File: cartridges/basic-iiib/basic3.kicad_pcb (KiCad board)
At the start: 2 copper layers, 72 x 37.3 mm, 10 parts, among them SW1 SW_SPDT, U1 27C512, U2 SG-1000-Cart, U3 UM61512

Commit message: Plotted - v0.1 released
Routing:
- net /GND: track 37.2 -> 62.5 mm, vias 6 -> 7
- net /D6: track 104.7 -> 105.8 mm
- removed copper zone on F.Cu, net /GND
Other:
- board size 72 x 37.3 mm -> 72 x 39.8 mm
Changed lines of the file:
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@@
   (gr_rect (start 189.484 135.89) (end 116.713 122.809) (layer "B.Mask") (width 0.15) (fill solid))
   (gr_rect (start 189.484 122.809) (end 116.713 136.398) (layer "F.Mask") (width 0.15) (fill solid))
-  (gr_line (start 189.238 122.686) (end 189.23 86.995) (layer "Edge.Cuts") (width 0.1))
-  (gr_line (start 117.238 124.286) (end 117.2464 86.995) (layer "Edge.Cuts") (width 0.1))
-  (gr_line (start 117.2464 86.995) (end 189.23 86.995) (layer "Edge.Cuts") (width 0.1))
+  (gr_line (start 189.238 122.686) (end 189.23 84.455) (layer "Edge.Cuts") (width 0.1))
+  (gr_line (start 117.238 124.286) (end 117.2464 84.455) (layer "Edge.Cuts") (width 0.1))
+  (gr_line (start 117.2464 84.455) (end 189.23 84.455) (layer "Edge.Cuts") (width 0.1))
   (gr_line (start 189.238 122.686) (end 189.238 124.286) (layer "Edge.Cuts") (width 0.1))
   (gr_text "A22" (at 186.436 120.904) (layer "B.SilkS")
@@
   (segment (start 172.72 113.665) (end 173.355 113.03) (width 0.75) (layer "B.Cu") (net 1))
   (segment (start 168.91 104.79) (end 172.07 104.79) (width 0.75) (layer "F.Cu") (net 2))
+  (segment (start 184.785 116.84) (end 183.515 116.84) (width 0.75) (layer "F.Cu") (net 2))
+  (segment (start 183.515 127.909) (end 183.338 128.086) (width 0.75) (layer "F.Cu") (net 2))
   (segment (start 172.07 104.79) (end 172.085 104.775) (width 0.75) (layer "F.Cu") (net 2))
+  (segment (start 186.518 128.086) (end 186.518 117.303) (width 0.75) (layer "F.Cu") (net 2))
   (segment (start 172.085 104.775) (end 177.8 104.775) (width 0.75) (layer "F.Cu") (net 2))
-  (via (at 183.515 116.84) (size 0.8) (drill 0.4) (layers "F.Cu" "B.Cu") (free) (net 2))
-  (via (at 183.515 118.11) (size 0.8) (drill 0.4) (layers "F.Cu" "B.Cu") (free) (net 2))
-  (via (at 186.055 118.11) (size 0.8) (drill 0.4) (layers "F.Cu" "B.Cu") (free) (net 2))
-  (via (at 186.055 116.84) (size 0.8) (drill 0.4) (layers "F.Cu" "B.Cu") (free) (net 2))
+  (segment (start 186.055 116.84) (end 184.785 116.84) (width 0.75) (layer "F.Cu") (net 2))
+  (segment (start 183.515 116.84) (end 183.515 118.11) (width 0.75) (layer "F.Cu") (net 2))
+  (segment (start 183.515 119.38) (end 183.515 127.909) (width 0.75) (layer "F.Cu") (net 2))
+  (segment (start 183.515 118.11) (end 183.515 119.38) (width 0.75) (layer "F.Cu") (net 2))
+  (segment (start 186.518 117.303) (end 186.055 116.84) (width 0.75) (layer "F.Cu") (net 2))
+  (via (at 183.515 119.38) (size 0.8) (drill 0.4) (layers "F.Cu" "B.Cu") (net 2))
+  (via (at 183.515 118.11) (size 0.8) (drill 0.4) (layers "F.Cu" "B.Cu") (net 2))
+  (via (at 186.055 116.84) (size 0.8) (drill 0.4) (layers "F.Cu" "B.Cu") (net 2))
+  (via (at 183.515 116.84) (size 0.8) (drill 0.4) (layers "F.Cu" "B.Cu") (net 2))
   (via (at 177.8 104.775) (size 0.8) (drill 0.4) (layers "F.Cu" "B.Cu") (net 2))
+  (via (at 184.785 116.84) (size 0.8) (drill 0.4) (layers "F.Cu" "B.Cu") (net 2))
   (via (at 172.085 104.775) (size 0.8) (drill 0.4) (layers "F.Cu" "B.Cu") (net 2))
   (segment (start 124.990489 94.739511) (end 126.365 93.365) (width 0.75) (layer "B.Cu") (net 2))
@@
   (via (at 186.69 97.79) (size 0.8) (drill 0.4) (layers "F.Cu" "B.Cu") (net 10))
   (via (at 136.525 97.79) (size 0.8) (drill 0.4) (layers "F.Cu" "B.Cu") (net 10))
+  (segment (start 183.96451 120.83549) (end 184.785 120.015) (width 0.25) (layer "B.Cu") (net 10))
   (segment (start 136.515 105.42) (end 136.515 118.74) (width 0.25) (layer "B.Cu") (net 10))
-  (segment (start 182.88 121.92) (end 184.785 120.015) (width 0.25) (layer "B.Cu") (net 10))
   (segment (start 136.525 99.695) (end 136.525 101.9197) (width 0.25) (layer "B.Cu") (net 10))
-  (segment (start 181.61 121.92) (end 182.88 121.92) (width 0.25) (layer "B.Cu") (net 10))
-  (segment (start 184.785 120.015) (end 186.055 120.015) (width 0.25) (layer "B.Cu") (net 10))
+  (segment (start 180.158 128.086) (end 180.158 123.372) (width 0.25) (layer "B.Cu") (net 10))
   (segment (start 136.525 97.79) (end 136.525 99.695) (width 0.25) (layer "B.Cu") (net 10))
-  (segment (start 180.158 123.372) (end 181.61 121.92) (width 0.25) (layer "B.Cu") (net 10))
+  (segment (start 180.158 123.372) (end 182.69451 120.83549) (width 0.25) (layer "B.Cu") (net 10))
   (segment (start 137.639511 103.034211) (end 137.639511 104.295489) (width 0.25) (layer "B.Cu") (net 10))
   (segment (start 136.525 101.9197) (end 137.639511 103.034211) (width 0.25) (layer "B.Cu") (net 10))
-  (segment (start 187.325 118.745) (end 187.325 98.425) (width 0.25) (layer "B.Cu") (net 10))
+  (segment (start 182.69451 120.83549) (end 183.96451 120.83549) (width 0.25) (layer "B.Cu") (net 10))
   (segment (start 187.325 98.425) (end 186.69 97.79) (width 0.25) (layer "B.Cu") (net 10))
-  (segment (start 180.158 128.086) (end 180.158 123.372) (width 0.25) (layer "B.Cu") (net 10))
   (segment (start 186.055 120.015) (end 187.325 118.745) (width 0.25) (layer "B.Cu") (net 10))
   (segment (start 137.639511 104.295489) (end 136.515 105.42) (width 0.25) (layer "B.Cu") (net 10))
+  (segment (start 184.785 120.015) (end 186.055 120.015) (width 0.25) (layer "B.Cu") (net 10))
+  (segment (start 187.325 118.745) (end 187.325 98.425) (width 0.25) (layer "B.Cu") (net 10))
   (segment (start 181.9996 96.52) (end 181.2751 97.2445) (width 0.25) (layer "F.Cu") (net 11))
   (segment (start 187.325 96.52) (end 181.9996 96.52) (width 0.25) (layer "F.Cu") (net 11))
@@
   (segment (start 140.179511 103.034211) (end 140.179511 104.295489) (width 0.25) (layer "B.Cu") (net 11))
   (segment (start 140.179511 104.295489) (end 139.055 105.42) (width 0.25) (layer "B.Cu") (net 11))
-  (segment (start 183.338 124.002704) (end 187.77451 119.566194) (width 0.25) (layer "B.Cu") (net 11))
+  (segment (start 187.77451 119.566194) (end 187.77451 119.56549) (width 0.25) (layer "B.Cu") (net 11))
+  (segment (start 184.15 121.285) (end 186.055704 121.285) (width 0.25) (layer "B.Cu") (net 11))
   (segment (start 187.96 119.38) (end 187.96 97.155) (width 0.25) (layer "B.Cu") (net 11))
   (segment (start 139.065 101.9197) (end 140.179511 103.034211) (width 0.25) (layer "B.Cu") (net 11))
-  (segment (start 187.77451 119.566194) (end 187.77451 119.56549) (width 0.25) (layer "B.Cu") (net 11))
   (segment (start 139.065 99.695) (end 139.065 101.9197) (width 0.25) (layer "B.Cu") (net 11))
-  (segment (start 183.338 128.086) (end 183.338 124.002704) (width 0.25) (layer "B.Cu") (net 11))
+  (segment (start 186.055704 121.285) (end 187.77451 119.566194) (width 0.25) (layer "B.Cu") (net 11))
+  (segment (start 187.96 97.155) (end 187.325 96.52) (width 0.25) (layer "B.Cu") (net 11))
+  (segment (start 183.338 128.086) (end 183.338 122.097) (width 0.25) (layer "B.Cu") (net 11))
   (segment (start 139.065 99.695) (end 139.065 97.2445) (width 0.25) (layer "B.Cu") (net 11))
   (segment (start 187.77451 119.56549) (end 187.96 119.38) (width 0.25) (layer "B.Cu") (net 11))
+  (segment (start 183.338 122.097) (end 184.15 121.285) (width 0.25) (layer "B.Cu") (net 11))
   (segment (start 139.055 105.42) (end 139.055 118.74) (width 0.25) (layer "B.Cu") (net 11))
-  (segment (start 187.96 97.155) (end 187.325 96.52) (width 0.25) (layer "B.Cu") (net 11))
   (segment (start 188.595 93.98) (end 141.605 93.98) (width 0.25) (layer "F.Cu") (net 12))
   (via (at 188.595 93.98) (size 0.8) (drill 0.4) (layers "F.Cu" "B.Cu") (net 12))
@@
   (segment (start 177.165 120.015) (end 177.609726 120.015) (width 0.25) (layer "B.Cu") (net 44))
   (segment (start 177.609726 120.015) (end 180.34 117.284726) (width 0.25) (layer "B.Cu") (net 44))
-  (zone (net 2) (net_name "/GND") (layer "F.Cu") (hatch edge 0.508)
-    (connect_pads yes (clearance 0.508))
-    (min_thickness 0.254) (filled_areas_thickness no)
-    (fill yes (thermal_gap 0.508) (thermal_bridge_width 0.508))
-    (polygon
-      (pts
-        (xy 187.452 128.016)
-        (xy 185.674 128.016)
-        (xy 185.674 121.412)
-        (xy 184.15 121.412)
-        (xy 184.15 128.905)
-        (xy 182.499 128.905)
-        (xy 182.499 115.824)
-        (xy 187.452 115.824)
-      )
-    )
-  )
   (zone (net 1) (net_name "/5V") (layer "F.Cu") (hatch edge 0.508)
     (connect_pads (clearance 0.508))
@@
         (xy 189.23 121.92)
         (xy 116.84 121.92)
-        (xy 116.84 86.36)
-        (xy 189.23 86.36)
+        (xy 116.84 80.01)
+        (xy 189.23 80.01)
       )
     )
@@
         (xy 189.23 121.92)
         (xy 116.84 121.92)
-        (xy 116.84 86.36)
-        (xy 189.23 86.36)
+        (xy 116.84 80.01)
+        (xy 189.23 80.01)
       )
     )

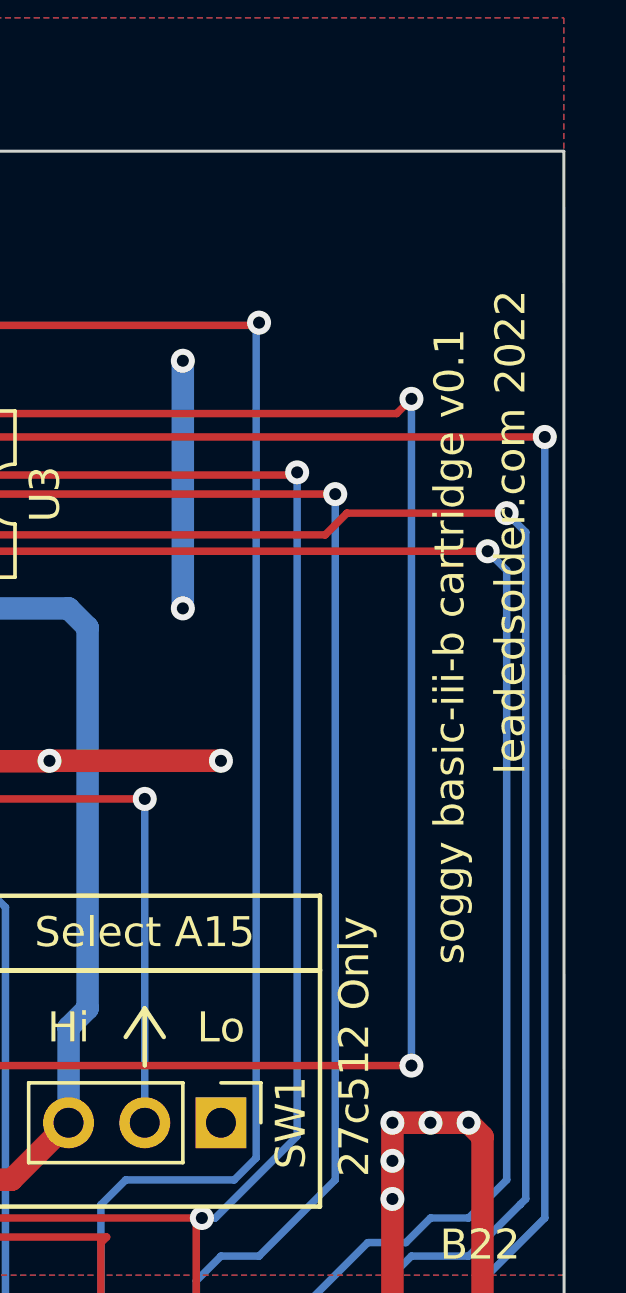
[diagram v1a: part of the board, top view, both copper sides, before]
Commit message: Jumper instructions on IIIB cart
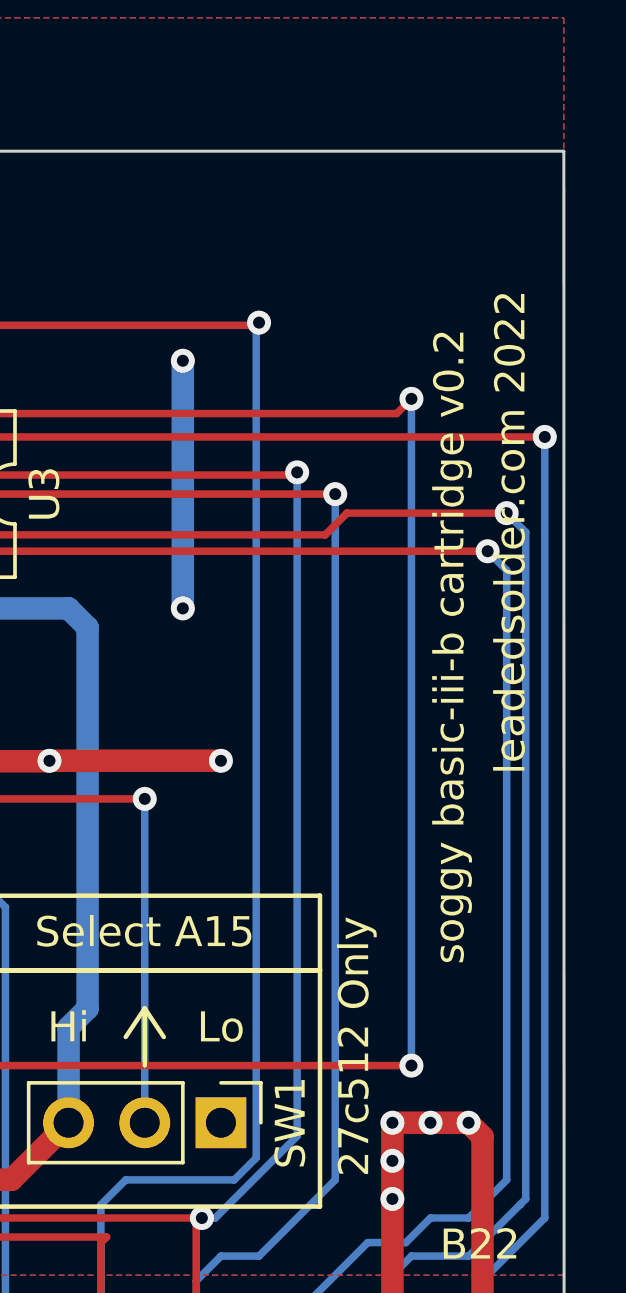
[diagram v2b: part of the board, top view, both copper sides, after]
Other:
- board text added: "Cut JP1 to disable 5V passthrough to B2 Cut JP3 to de-inhibit system RAM decode"
- board text added: "soggy basic-iii-b cartridge v0.2"
- board text removed: "soggy basic-iii-b cartridge v0.1"
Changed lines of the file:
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@@
+    (effects (font (size 1 1) (thickness 0.15)) (justify mirror))
+  )
+  (gr_text "Cut JP1 to disable 5V passthrough to B2\nCut JP3 to de-inhibit system RAM decode" (at 172.212 86.868) (layer "B.SilkS")
     (effects (font (size 1 1) (thickness 0.15)) (justify mirror))
   )
@@
     (effects (font (size 1 1) (thickness 0.15)))
   )
-  (gr_text "soggy basic-iii-b cartridge v0.1" (at 185.42 100.965 90) (layer "F.SilkS")
+  (gr_text "soggy basic-iii-b cartridge v0.2" (at 185.42 100.965 90) (layer "F.SilkS")
     (effects (font (size 1 1) (thickness 0.15)))
   )

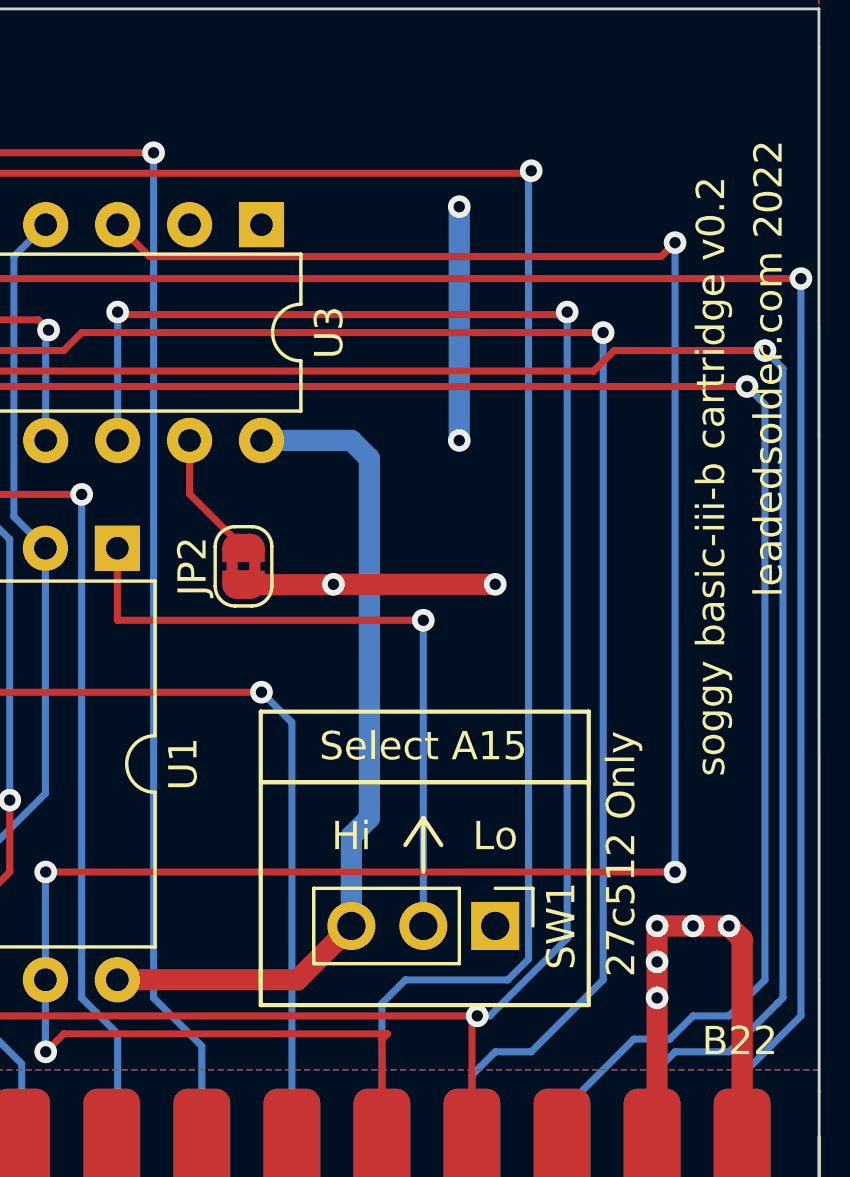
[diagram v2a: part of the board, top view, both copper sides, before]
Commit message: Carts to KiCad 7
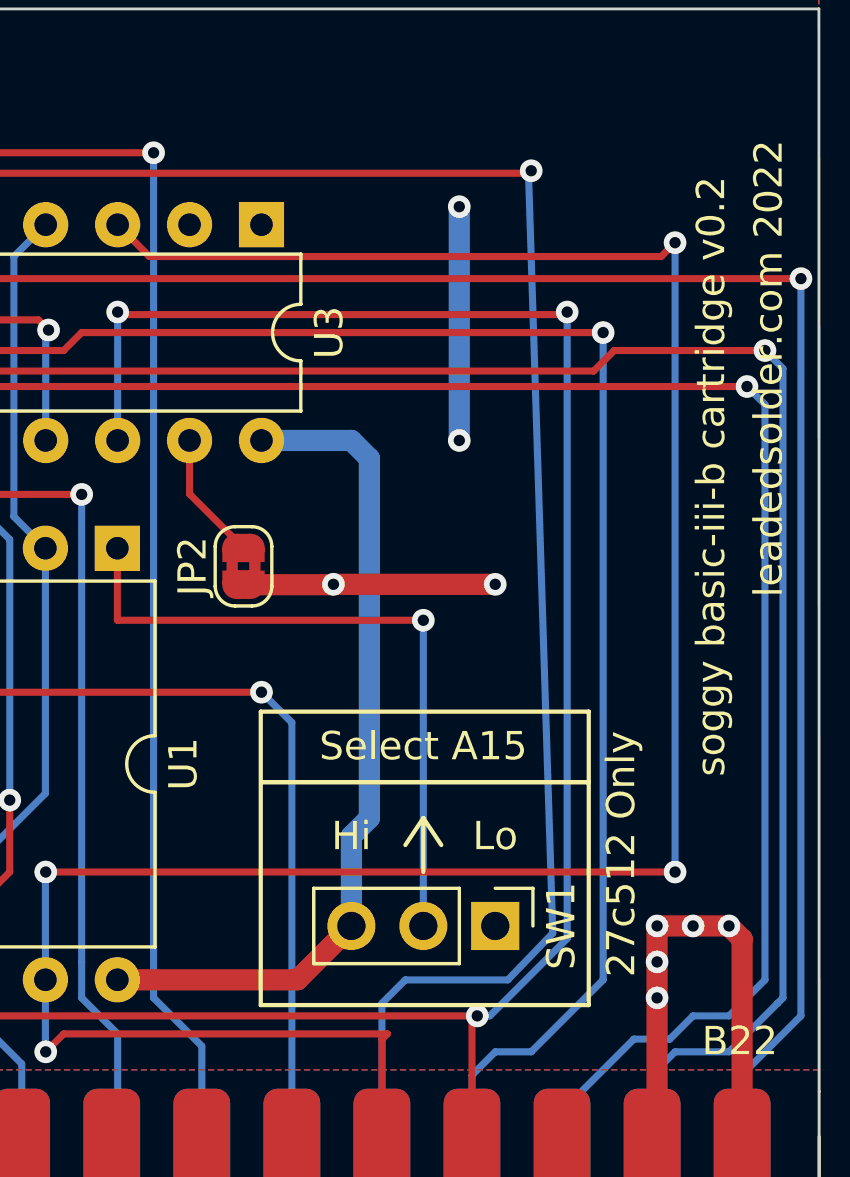
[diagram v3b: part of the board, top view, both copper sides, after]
